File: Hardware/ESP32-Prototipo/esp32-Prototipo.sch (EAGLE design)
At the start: 42 parts, among them M1 BATTERY-CHARGER-LI-PROT, T1 BC847, U21 DC-DC-STEP-UP

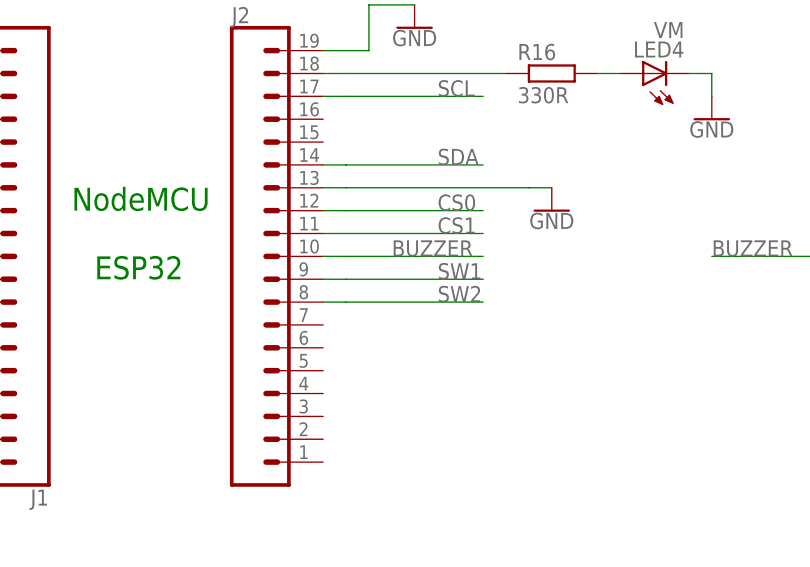
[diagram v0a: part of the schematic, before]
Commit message: Buzzer -> GPIO04
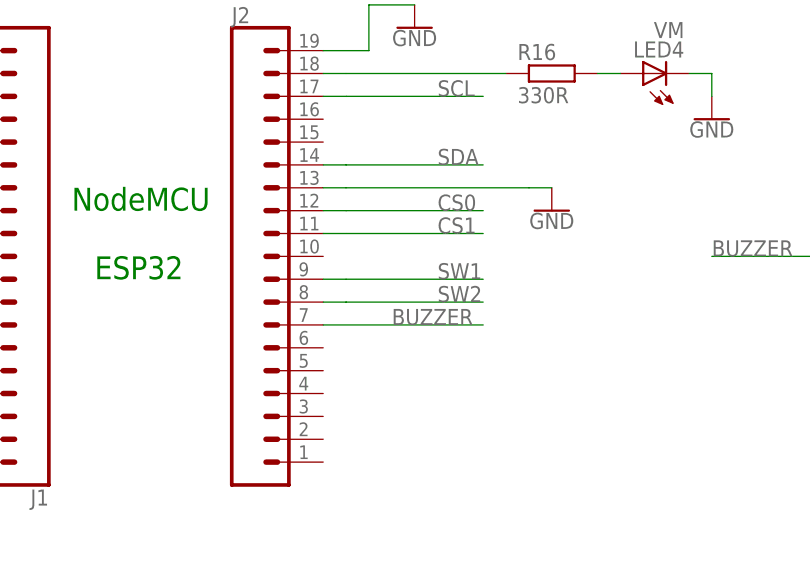
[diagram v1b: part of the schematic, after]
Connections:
- net BUZZER: now also J2.7; no longer J2.10
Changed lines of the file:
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@@
 <net name="BUZZER" class="0">
-<segment>
-<wire x1="132.08" y1="139.7" x2="147.32" y2="139.7" width="0.1524" layer="91"/>
-<label x="137.16" y="139.7" size="1.778" layer="95"/>
-<pinref part="J2" gate="G$1" pin="10"/>
-<wire x1="129.54" y1="139.7" x2="132.08" y2="139.7" width="0.1524" layer="91"/>
-</segment>
 <segment>
 <pinref part="R17" gate="G$1" pin="1"/>
@@
 <label x="172.72" y="139.7" size="1.778" layer="95"/>
 </segment>
+<segment>
+<pinref part="J2" gate="G$1" pin="7"/>
+<wire x1="129.54" y1="132.08" x2="147.32" y2="132.08" width="0.1524" layer="91"/>
+<label x="137.16" y="132.08" size="1.778" layer="95"/>
+</segment>
 </net>
